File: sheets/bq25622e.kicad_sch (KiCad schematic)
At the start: 15 parts, among them U4 BQ25628E

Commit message: Fix warnings
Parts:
- removed U4: BQ25628E, PowerFeather:BQ25629, symbol PowerFeather:BQ25628E
- added U4: BQ25628E, PowerFeather:BQ25628E, symbol PowerFeather_KiCAD_Lib:BQ25628E
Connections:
- net CE: now also U4.14 (~{CE})
- net GND: now also U4.15 (GND)
- net ILIM: now also U4.4 (ILIM)
- net INT: now also U4.11 (~{INT})
- net PG: now also U4.3 (PMID_GD)
- net QON: now also U4.7 (~{QON})
- net SCL: now also U4.13 (SCL)
- net SDA: now also U4.12 (SDA)
- net TS: now also U4.6 (TS)
- net VBAT: now also U4.8 (BAT)
- net VIN: now also U4.18 (VBUS)
- net VSYS: now also U4.9 (SYS)
- net at C11.1, L1.1: now also U4.16 (SW)
- net at C11.2: now also U4.1 (BTST)
- net at R21.2: now also U4.10 (STAT)
- net at C6.1, C7.1: now also U4.17 (PMID)
- net at C12.2: now also U4.2 (REGN)
- net at R22.2: now also U4.5 (TS_BIAS)

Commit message: Fix warnings
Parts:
- LED2: footprint PowerFeather:LED_0603_1608Metric -> LED_SMD:LED_0603_1608Metric
- U4: footprint PowerFeather:BQ25628E -> PowerFeather_KiCAD_Lib:BQ25628E
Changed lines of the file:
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@@
 			)
 		)
-		(property "Footprint" "PowerFeather:LED_0603_1608Metric"
+		(property "Footprint" "LED_SMD:LED_0603_1608Metric"
 			(at 63.5 49.53 0)
 			(effects
@@
 			)
 		)
-		(property "Footprint" "PowerFeather:BQ25628E"
+		(property "Footprint" "PowerFeather_KiCAD_Lib:BQ25628E"
 			(at 102.108 83.312 0)
 			(effects

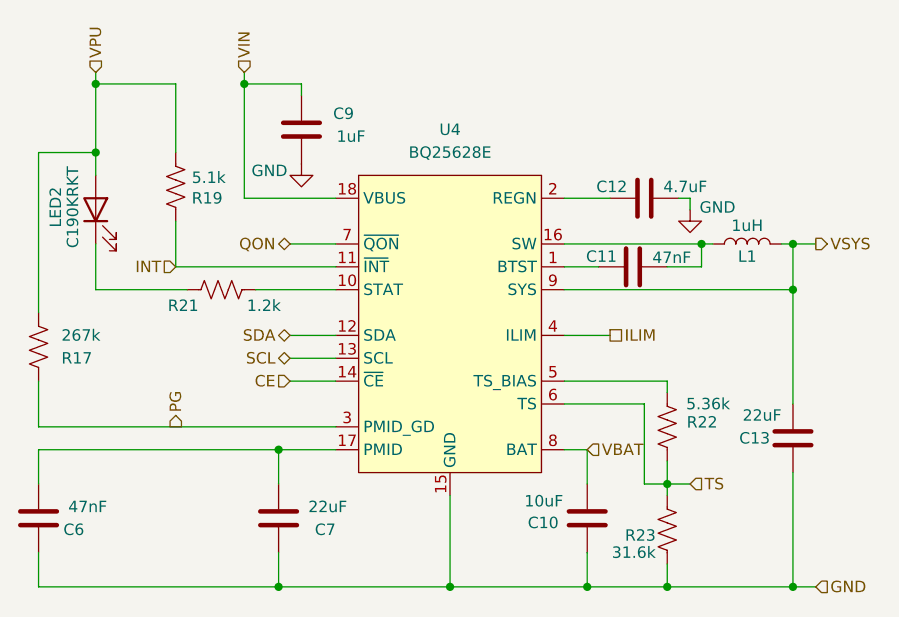
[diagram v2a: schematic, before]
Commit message: Renumber components for powerups
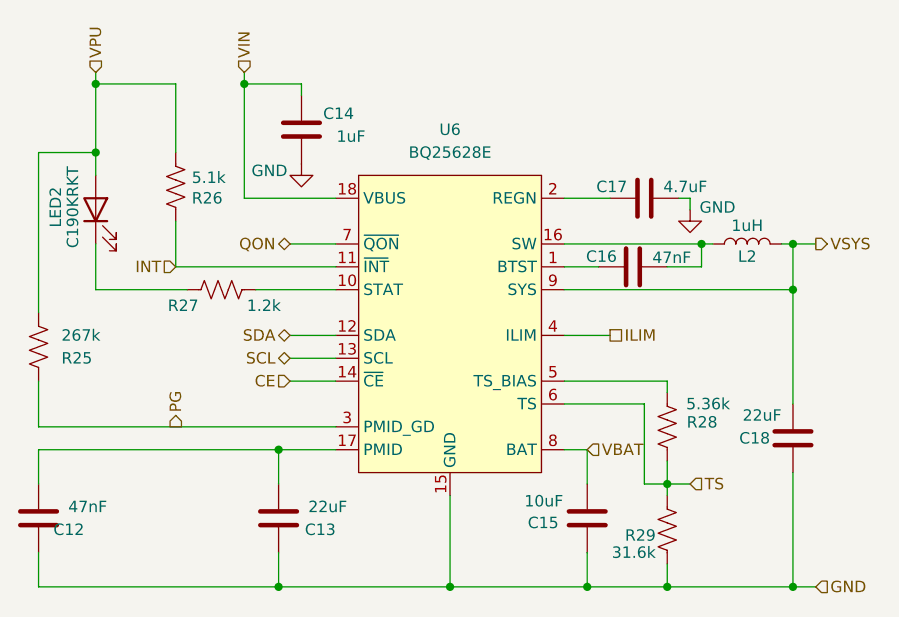
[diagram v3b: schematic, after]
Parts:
- renumbered C6 to C12, C7 to C13, C9 to C14, C10 to C15, C11 to C16, C12 to C17, C13 to C18, L1 to L2, R17 to R25, R19 to R26, R21 to R27, R22 to R28, R23 to R29, U4 to U6
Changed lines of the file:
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@@
 		(on_board yes)
 		(dnp no)
-		(property "Reference" "C11"
+		(property "Reference" "C16"
 			(at 121.412 54.737 90)
 			(effects
@@
 			(project "powerups"
 				(path "/351775ff-22dd-4601-a146-0ae5bb7b1807/788c158d-fb18-46fd-a4f8-fb3433f7b73b"
-					(reference "C11")
+					(reference "C16")
 					(unit 1)
 				)
@@
 		(on_board yes)
 		(dnp no)
-		(property "Reference" "C10"
+		(property "Reference" "C15"
 			(at 111.506 84.328 0)
 			(effects
@@
 			(project "powerups"
 				(path "/351775ff-22dd-4601-a146-0ae5bb7b1807/788c158d-fb18-46fd-a4f8-fb3433f7b73b"
-					(reference "C10")
+					(reference "C15")
 					(unit 1)
 				)
@@
 		(on_board yes)
 		(dnp no)
-		(property "Reference" "R17"
+		(property "Reference" "R25"
 			(at 59.69 66.04 0)
 			(effects
@@
 			(project "powerups"
 				(path "/351775ff-22dd-4601-a146-0ae5bb7b1807/788c158d-fb18-46fd-a4f8-fb3433f7b73b"
-					(reference "R17")
+					(reference "R25")
 					(unit 1)
 				)
@@
 		(on_board yes)
 		(dnp no)
-		(property "Reference" "R21"
+		(property "Reference" "R27"
 			(at 74.93 60.198 90)
 			(effects
@@
 			(project "powerups"
 				(path "/351775ff-22dd-4601-a146-0ae5bb7b1807/788c158d-fb18-46fd-a4f8-fb3433f7b73b"
-					(reference "R21")
+					(reference "R27")
 					(unit 1)
 				)
@@
 		(on_board yes)
 		(dnp no)
-		(property "Reference" "L1"
+		(property "Reference" "L2"
 			(at 135.89 54.737 90)
 			(effects
@@
 			(project "powerups"
 				(path "/351775ff-22dd-4601-a146-0ae5bb7b1807/788c158d-fb18-46fd-a4f8-fb3433f7b73b"
-					(reference "L1")
+					(reference "L2")
 					(unit 1)
 				)
@@
 		(on_board yes)
 		(dnp no)
-		(property "Reference" "C13"
+		(property "Reference" "C18"
 			(at 138.43 74.93 0)
 			(effects
@@
 			(project "powerups"
 				(path "/351775ff-22dd-4601-a146-0ae5bb7b1807/788c158d-fb18-46fd-a4f8-fb3433f7b73b"
-					(reference "C13")
+					(reference "C18")
 					(unit 1)
 				)
@@
 		(on_board yes)
 		(dnp no)
-		(property "Reference" "R19"
+		(property "Reference" "R26"
 			(at 74.168 48.26 0)
 			(effects
@@
 			(project "powerups"
 				(path "/351775ff-22dd-4601-a146-0ae5bb7b1807/788c158d-fb18-46fd-a4f8-fb3433f7b73b"
-					(reference "R19")
+					(reference "R26")
 					(unit 1)
 				)
@@
 		(on_board yes)
 		(dnp no)
-		(property "Reference" "#PWR08"
+		(property "Reference" "#PWR022"
 			(at 129.54 55.88 0)
 			(effects
@@
 			(project "powerups"
 				(path "/351775ff-22dd-4601-a146-0ae5bb7b1807/788c158d-fb18-46fd-a4f8-fb3433f7b73b"
-					(reference "#PWR08")
+					(reference "#PWR022")
 					(unit 1)
 				)
@@
 		(on_board yes)
 		(dnp no)
-		(property "Reference" "C6"
+		(property "Reference" "C12"
 			(at 62.23 85.09 0)
 			(effects
@@
 			(project "powerups"
 				(path "/351775ff-22dd-4601-a146-0ae5bb7b1807/788c158d-fb18-46fd-a4f8-fb3433f7b73b"
-					(reference "C6")
+					(reference "C12")
 					(unit 1)
 				)
@@
 		(on_board yes)
 		(dnp no)
-		(property "Reference" "C7"
+		(property "Reference" "C13"
 			(at 90.17 85.09 0)
 			(effects
@@
 			(project "powerups"
 				(path "/351775ff-22dd-4601-a146-0ae5bb7b1807/788c158d-fb18-46fd-a4f8-fb3433f7b73b"
-					(reference "C7")
+					(reference "C13")
 					(unit 1)
 				)
@@
 		(on_board yes)
 		(dnp no)
-		(property "Reference" "R22"
+		(property "Reference" "R28"
 			(at 132.588 73.152 0)
 			(effects
@@
 			(project "powerups"
 				(path "/351775ff-22dd-4601-a146-0ae5bb7b1807/788c158d-fb18-46fd-a4f8-fb3433f7b73b"
-					(reference "R22")
+					(reference "R28")
 					(unit 1)
 				)
@@
 		(on_board yes)
 		(dnp no)
-		(property "Reference" "R23"
+		(property "Reference" "R29"
 			(at 125.73 85.725 0)
 			(effects
@@
 			(project "powerups"
 				(path "/351775ff-22dd-4601-a146-0ae5bb7b1807/788c158d-fb18-46fd-a4f8-fb3433f7b73b"
-					(reference "R23")
+					(reference "R29")
 					(unit 1)
 				)
@@
 		(on_board yes)
 		(dnp no)
-		(property "Reference" "#PWR07"
+		(property "Reference" "#PWR021"
 			(at 86.36 50.8 0)
 			(effects
@@
 			(project ""
 				(path "/351775ff-22dd-4601-a146-0ae5bb7b1807/788c158d-fb18-46fd-a4f8-fb3433f7b73b"
-					(reference "#PWR07")
+					(reference "#PWR021")
 					(unit 1)
 				)
@@
 		(dnp no)
 		(fields_autoplaced yes)
-		(property "Reference" "U4"
+		(property "Reference" "U6"
 			(at 102.87 40.64 0)
 			(effects
@@
 			(project ""
 				(path "/351775ff-22dd-4601-a146-0ae5bb7b1807/788c158d-fb18-46fd-a4f8-fb3433f7b73b"
-					(reference "U4")
+					(reference "U6")
 					(unit 1)
 				)
@@
 		(on_board yes)
 		(dnp no)
-		(property "Reference" "C9"
+		(property "Reference" "C14"
 			(at 92.202 38.862 0)
 			(effects
@@
 			(project "powerups"
 				(path "/351775ff-22dd-4601-a146-0ae5bb7b1807/788c158d-fb18-46fd-a4f8-fb3433f7b73b"
-					(reference "C9")
+					(reference "C14")
 					(unit 1)
 				)
@@
 		(on_board yes)
 		(dnp no)
-		(property "Reference" "C12"
+		(property "Reference" "C17"
 			(at 122.555 46.99 90)
 			(effects
@@
 			(project "powerups"
 				(path "/351775ff-22dd-4601-a146-0ae5bb7b1807/788c158d-fb18-46fd-a4f8-fb3433f7b73b"
-					(reference "C12")
-					(unit 1)
-				)
+					(reference "C17")
+					(unit 1)
+				)

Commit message: Remove unecessary symbols
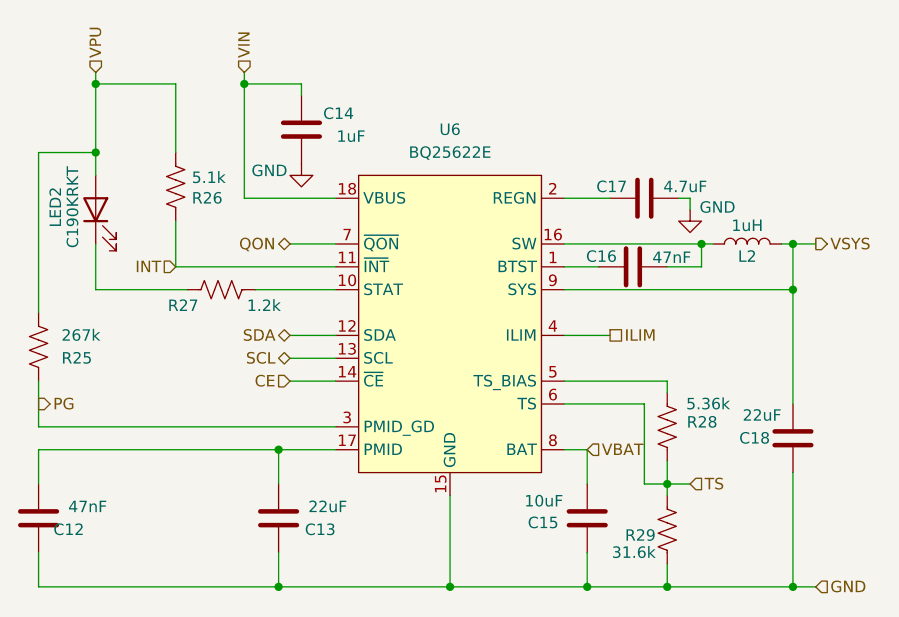
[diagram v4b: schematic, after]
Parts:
- U6: value BQ25628E -> BQ25622E; footprint PowerFeather_KiCAD_Lib:BQ25628E -> PowerFeather_KiCAD_Lib:BQ25622E; symbol PowerFeather_KiCAD_Lib:BQ25628E -> PowerFeather_KiCAD_Lib:BQ25622E
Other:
- company: (none) -> PowerFeather
- title: (none) -> BQ25622E charger circuit
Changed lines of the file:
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@@
 	(generator_version "8.0")
 	(paper "A5")
+	(title_block
+		(title "BQ25622E charger circuit")
+		(date "2024-10-11")
+		(rev "0.9.0")
+		(company "PowerFeather")
+	)
 	(junction
 		(at 118.11 91.44)
@@
 	)
 	(image
-		(at 96.012 111.506)
+		(at 96.52 110.236)
 		(scale 0.0917897)
 		(data "iVBORw0KGgoAAAANSUhEUgAAAgAAAAIACAYAAAD0eNT6AAAABHNCSVQICAgIfAhkiAAAAAlwSFlz"
@@
 	(hierarchical_label "PG"
 		(shape output)
-		(at 72.39 73.66 90)
+		(at 57.15 71.12 0)
 		(fields_autoplaced yes)
 		(effects
@@
 	)
 	(symbol
-		(lib_id "PowerFeather_KiCAD_Lib:BQ25628E")
+		(lib_id "PowerFeather_KiCAD_Lib:BQ25622E")
 		(at 102.87 63.5 0)
 		(unit 1)
@@
 			)
 		)
-		(property "Value" "BQ25628E"
+		(property "Value" "BQ25622E"
 			(at 102.87 43.18 0)
 			(effects
@@
 			)
 		)
-		(property "Footprint" "PowerFeather_KiCAD_Lib:BQ25628E"
+		(property "Footprint" "PowerFeather_KiCAD_Lib:BQ25622E"
 			(at 102.108 83.312 0)
 			(effects

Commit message: Some cleanup
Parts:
- R26: value 5.1k -> 5.36k; MPN 603-AC0402FR-075K1L -> 603-RT0402BRD075K36L
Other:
- moved on the sheet: R29
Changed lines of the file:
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@@
 	(wire
 		(pts
-			(xy 115.57 63.5) (xy 120.65 63.5)
+			(xy 115.57 63.5) (xy 125.73 63.5)
 		)
 		(stroke
@@
 	(hierarchical_label "ILIM"
 		(shape passive)
-		(at 120.65 63.5 0)
+		(at 125.73 63.5 0)
 		(fields_autoplaced yes)
 		(effects
@@
 		(lib_id "Device:C")
 		(at 140.97 74.93 0)
+		(mirror y)
 		(unit 1)
 		(exclude_from_sim no)
@@
 		(dnp no)
 		(property "Reference" "C18"
-			(at 138.43 74.93 0)
+			(at 143.51 75.946 0)
 			(effects
 				(font
@@
 		)
 		(property "Value" "22uF"
-			(at 139.7 72.39 0)
+			(at 143.764 73.406 0)
 			(effects
 				(font
@@
 		)
 		(property "Footprint" "Capacitor_SMD:C_0805_2012Metric"
-			(at 141.9352 78.74 0)
+			(at 140.0048 78.74 0)
 			(effects
 				(font
@@
 			)
 		)
-		(property "Value" "5.1k"
+		(property "Value" "5.36k"
 			(at 74.168 45.974 0)
 			(effects
@@
 			)
 		)
-		(property "MPN" "603-AC0402FR-075K1L"
+		(property "MPN" "603-RT0402BRD075K36L"
 			(at 72.39 46.99 0)
 			(effects
@@
 		(dnp no)
 		(property "Reference" "R28"
-			(at 132.588 73.152 0)
+			(at 132.588 74.93 0)
 			(effects
 				(font
@@
 		)
 		(property "Value" "5.36k"
-			(at 133.985 71.12 0)
+			(at 134.112 72.644 0)
 			(effects
 				(font
@@
 	(symbol
 		(lib_id "Device:R_US")
-		(at 127 85.09 180)
+		(at 127 85.09 0)
+		(mirror x)
 		(unit 1)
 		(exclude_from_sim no)
@@
 		(dnp no)
 		(property "Reference" "R29"
-			(at 125.73 85.725 0)
+			(at 128.27 84.328 0)
 			(effects
 				(font
@@
 		)
 		(property "Value" "31.6k"
-			(at 125.73 87.63 0)
+			(at 128.27 86.614 0)
 			(effects
 				(font
@@
 		)
 		(property "Footprint" "Resistor_SMD:R_0402_1005Metric"
-			(at 125.984 84.836 90)
-			(effects
-				(font
+			(at 128.016 84.836 90)
+			(effects
+				(font
